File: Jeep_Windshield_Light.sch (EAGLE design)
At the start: 9 parts

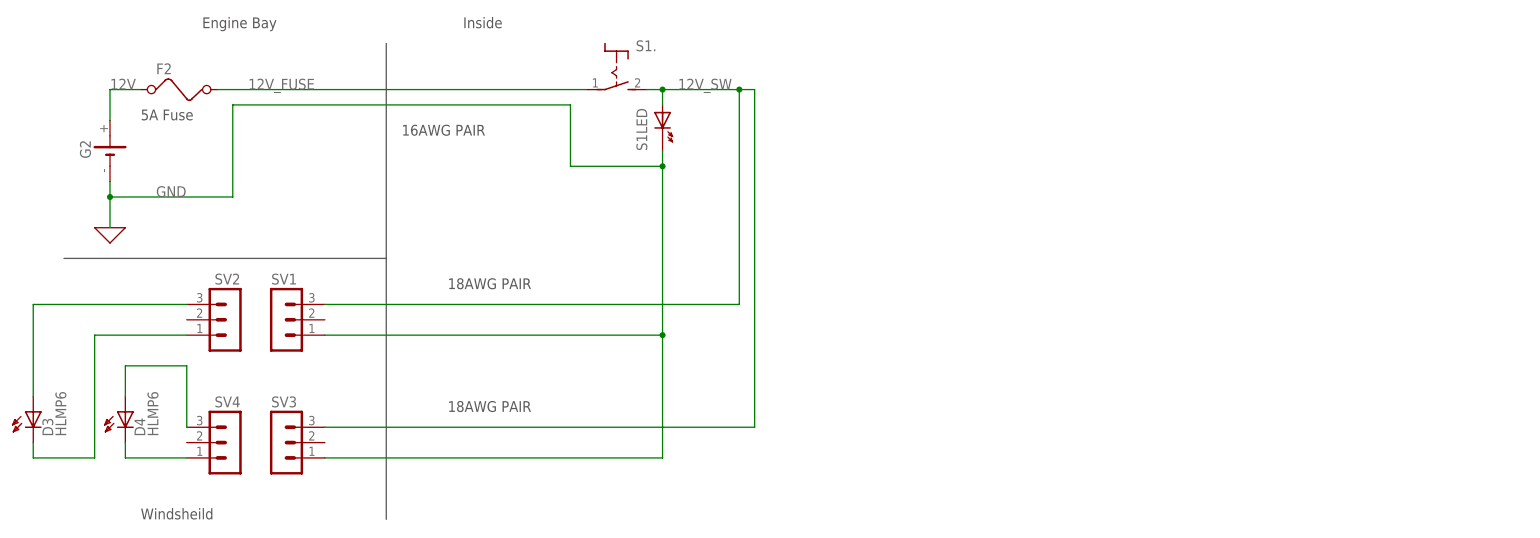
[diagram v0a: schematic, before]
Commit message: Updating grill version to include the ignition wiring. Also updating the original version to look consistent.
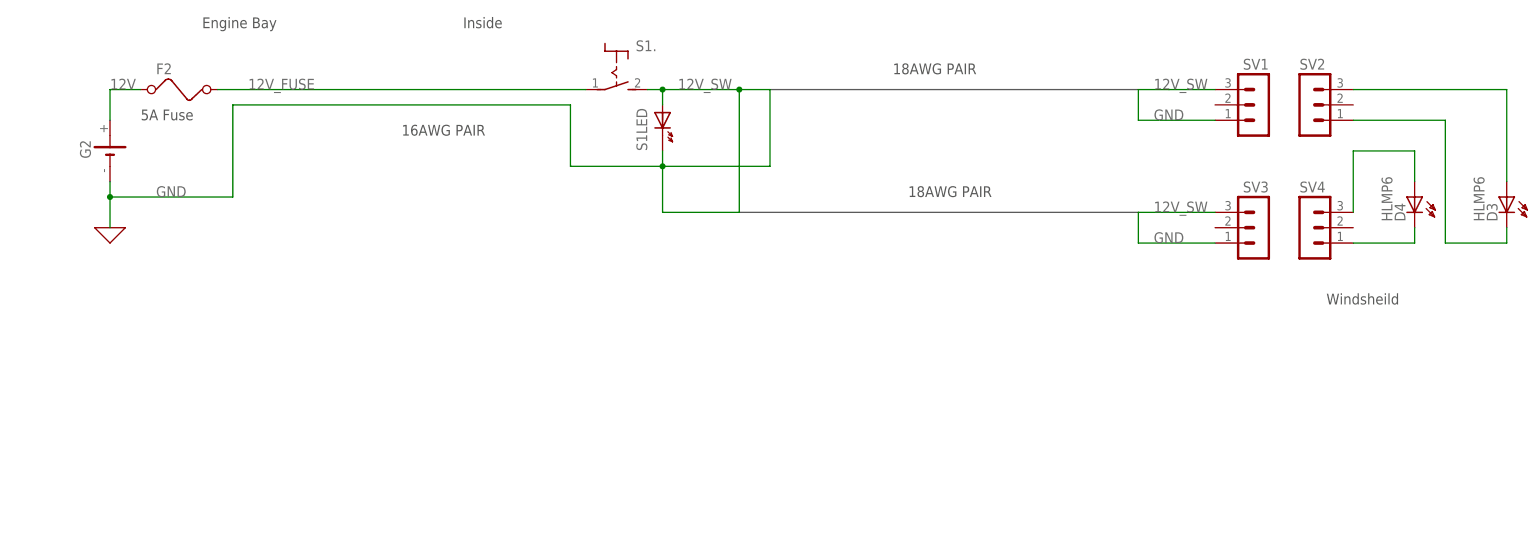
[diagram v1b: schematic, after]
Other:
- moved on the sheet: D3, D4, SV1, SV2, SV3, SV4
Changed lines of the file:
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@@
 <plain>
 <text x="22.86" y="63.5" size="1.778" layer="97">5A Fuse</text>
-<wire x1="63.5" y1="76.2" x2="63.5" y2="40.64" width="0.1524" layer="97"/>
 <text x="76.2" y="78.74" size="1.778" layer="97">Inside</text>
 <text x="33.02" y="78.74" size="1.778" layer="97">Engine Bay</text>
-<wire x1="63.5" y1="40.64" x2="63.5" y2="-2.54" width="0.1524" layer="97"/>
-<wire x1="10.16" y1="40.64" x2="63.5" y2="40.64" width="0.1524" layer="97"/>
-<text x="22.86" y="-2.54" size="1.778" layer="97">Windsheild</text>
+<text x="231.14" y="33.02" size="1.778" layer="97" rot="MR0">Windsheild</text>
 <text x="66.04" y="60.96" size="1.778" layer="97">16AWG PAIR</text>
-<text x="73.66" y="35.56" size="1.778" layer="97">18AWG PAIR</text>
-<text x="73.66" y="15.24" size="1.778" layer="97">18AWG PAIR</text>
+<text x="147.32" y="71.12" size="1.778" layer="97">18AWG PAIR</text>
+<text x="149.86" y="50.8" size="1.778" layer="97">18AWG PAIR</text>
 </plain>
 <instances>
@@
 <instance part="S1" gate="LED" x="109.22" y="63.5"/>
 <instance part="X_2" gate="G$1" x="17.78" y="45.72"/>
-<instance part="D3" gate="A" x="5.08" y="12.7"/>
-<instance part="D4" gate="A" x="20.32" y="12.7"/>
-<instance part="SV1" gate="G$1" x="45.72" y="30.48"/>
-<instance part="SV2" gate="G$1" x="38.1" y="30.48" rot="MR0"/>
-<instance part="SV3" gate="G$1" x="45.72" y="10.16"/>
-<instance part="SV4" gate="G$1" x="38.1" y="10.16" rot="MR0"/>
+<instance part="D3" gate="A" x="248.92" y="48.26" rot="MR0"/>
+<instance part="D4" gate="A" x="233.68" y="48.26" rot="MR0"/>
+<instance part="SV1" gate="G$1" x="208.28" y="66.04" rot="MR0"/>
+<instance part="SV2" gate="G$1" x="215.9" y="66.04"/>
+<instance part="SV3" gate="G$1" x="208.28" y="45.72" rot="MR0"/>
+<instance part="SV4" gate="G$1" x="215.9" y="45.72"/>
 </instances>
 <busses>
+<bus name="12V_SW,GND">
+<segment>
+<wire x1="127" y1="68.58" x2="187.96" y2="68.58" width="0.762" layer="92"/>
+</segment>
+<segment>
+<wire x1="121.92" y1="48.26" x2="187.96" y2="48.26" width="0.762" layer="92"/>
+</segment>
+</bus>
 </busses>
 <nets>
@@
 </segment>
 </net>
-<net name="12V_SW" class="0">
-<segment>
-<pinref part="S1" gate="." pin="S"/>
-<wire x1="106.68" y1="68.58" x2="109.22" y2="68.58" width="0.1524" layer="91"/>
-<wire x1="109.22" y1="68.58" x2="121.92" y2="68.58" width="0.1524" layer="91"/>
-<wire x1="109.22" y1="66.04" x2="109.22" y2="68.58" width="0.1524" layer="91"/>
-<junction x="109.22" y="68.58"/>
-<pinref part="S1" gate="LED" pin="A"/>
-<wire x1="121.92" y1="68.58" x2="121.92" y2="33.02" width="0.1524" layer="91"/>
-<wire x1="124.46" y1="68.58" x2="124.46" y2="12.7" width="0.1524" layer="91"/>
-<wire x1="124.46" y1="68.58" x2="121.92" y2="68.58" width="0.1524" layer="91"/>
-<junction x="121.92" y="68.58"/>
-<pinref part="SV1" gate="G$1" pin="3"/>
-<wire x1="53.34" y1="33.02" x2="121.92" y2="33.02" width="0.1524" layer="91"/>
-<pinref part="SV3" gate="G$1" pin="3"/>
-<wire x1="53.34" y1="12.7" x2="124.46" y2="12.7" width="0.1524" layer="91"/>
-<label x="111.76" y="68.58" size="1.778" layer="95"/>
-</segment>
-</net>
 <net name="GND" class="0">
 <segment>
@@
 <wire x1="17.78" y1="45.72" x2="17.78" y2="50.8" width="0.1524" layer="91"/>
 <junction x="17.78" y="50.8"/>
-<wire x1="109.22" y1="55.88" x2="109.22" y2="27.94" width="0.1524" layer="91"/>
 <junction x="109.22" y="55.88"/>
+<wire x1="109.22" y1="55.88" x2="109.22" y2="48.26" width="0.1524" layer="91"/>
+<wire x1="109.22" y1="55.88" x2="127" y2="55.88" width="0.1524" layer="91"/>
+<wire x1="127" y1="55.88" x2="127" y2="68.58" width="0.1524" layer="91"/>
+<wire x1="121.92" y1="48.26" x2="109.22" y2="48.26" width="0.1524" layer="91"/>
+</segment>
+<segment>
 <pinref part="SV1" gate="G$1" pin="1"/>
-<wire x1="53.34" y1="27.94" x2="109.22" y2="27.94" width="0.1524" layer="91"/>
+<wire x1="187.96" y1="63.5" x2="200.66" y2="63.5" width="0.1524" layer="91"/>
+<label x="190.5" y="63.5" size="1.778" layer="95"/>
+<wire x1="187.96" y1="63.5" x2="187.96" y2="68.58" width="0.1524" layer="91"/>
+</segment>
+<segment>
+<wire x1="187.96" y1="48.26" x2="187.96" y2="43.18" width="0.1524" layer="91"/>
 <pinref part="SV3" gate="G$1" pin="1"/>
-<wire x1="53.34" y1="7.62" x2="109.22" y2="7.62" width="0.1524" layer="91"/>
-<wire x1="109.22" y1="27.94" x2="109.22" y2="7.62" width="0.1524" layer="91"/>
-<junction x="109.22" y="27.94"/>
+<wire x1="187.96" y1="43.18" x2="200.66" y2="43.18" width="0.1524" layer="91"/>
+<label x="190.5" y="43.18" size="1.778" layer="95"/>
 </segment>
 </net>
@@
 <segment>
 <pinref part="D4" gate="A" pin="A"/>
-<wire x1="20.32" y1="22.86" x2="20.32" y2="17.78" width="0.1524" layer="91"/>
+<wire x1="233.68" y1="58.42" x2="233.68" y2="53.34" width="0.1524" layer="91"/>
 <pinref part="SV4" gate="G$1" pin="3"/>
-<wire x1="30.48" y1="12.7" x2="30.48" y2="22.86" width="0.1524" layer="91"/>
-<wire x1="30.48" y1="22.86" x2="20.32" y2="22.86" width="0.1524" layer="91"/>
+<wire x1="223.52" y1="48.26" x2="223.52" y2="58.42" width="0.1524" layer="91"/>
+<wire x1="223.52" y1="58.42" x2="233.68" y2="58.42" width="0.1524" layer="91"/>
 </segment>
 </net>
@@
 <pinref part="D3" gate="A" pin="A"/>
 <pinref part="SV2" gate="G$1" pin="3"/>
-<wire x1="30.48" y1="33.02" x2="5.08" y2="33.02" width="0.1524" layer="91"/>
-<wire x1="5.08" y1="33.02" x2="5.08" y2="17.78" width="0.1524" layer="91"/>
+<wire x1="223.52" y1="68.58" x2="248.92" y2="68.58" width="0.1524" layer="91"/>
+<wire x1="248.92" y1="68.58" x2="248.92" y2="53.34" width="0.1524" layer="91"/>
 </segment>
 </net>
@@
 <pinref part="D4" gate="A" pin="K"/>
 <pinref part="SV4" gate="G$1" pin="1"/>
-<wire x1="20.32" y1="7.62" x2="20.32" y2="10.16" width="0.1524" layer="91"/>
-<wire x1="30.48" y1="7.62" x2="20.32" y2="7.62" width="0.1524" layer="91"/>
+<wire x1="233.68" y1="43.18" x2="233.68" y2="45.72" width="0.1524" layer="91"/>
+<wire x1="223.52" y1="43.18" x2="233.68" y2="43.18" width="0.1524" layer="91"/>
 </segment>
 </net>
@@
 <segment>
 <pinref part="D3" gate="A" pin="K"/>
-<wire x1="5.08" y1="7.62" x2="5.08" y2="10.16" width="0.1524" layer="91"/>
+<wire x1="248.92" y1="43.18" x2="248.92" y2="45.72" width="0.1524" layer="91"/>
 <pinref part="SV2" gate="G$1" pin="1"/>
-<wire x1="30.48" y1="27.94" x2="15.24" y2="27.94" width="0.1524" layer="91"/>
-<wire x1="15.24" y1="27.94" x2="15.24" y2="7.62" width="0.1524" layer="91"/>
-<wire x1="15.24" y1="7.62" x2="5.08" y2="7.62" width="0.1524" layer="91"/>
+<wire x1="223.52" y1="63.5" x2="238.76" y2="63.5" width="0.1524" layer="91"/>
+<wire x1="238.76" y1="63.5" x2="238.76" y2="43.18" width="0.1524" layer="91"/>
+<wire x1="238.76" y1="43.18" x2="248.92" y2="43.18" width="0.1524" layer="91"/>
 </segment>
 </net>
+<net name="B$1" class="0">
+<segment>
+<wire x1="193.04" y1="68.58" x2="187.96" y2="68.58" width="0.1524" layer="91"/>
+</segment>
+</net>
+<net name="12V_SW" class="0">
+<segment>
+<pinref part="SV1" gate="G$1" pin="3"/>
+<wire x1="193.04" y1="68.58" x2="200.66" y2="68.58" width="0.1524" layer="91"/>
+<label x="190.5" y="68.58" size="1.778" layer="95"/>
+</segment>
+<segment>
+<pinref part="SV3" gate="G$1" pin="3"/>
+<wire x1="187.96" y1="48.26" x2="200.66" y2="48.26" width="0.1524" layer="91"/>
+<label x="190.5" y="48.26" size="1.778" layer="95"/>
+</segment>
+<segment>
+<pinref part="S1" gate="." pin="S"/>
+<wire x1="106.68" y1="68.58" x2="109.22" y2="68.58" width="0.1524" layer="91"/>
+<wire x1="109.22" y1="66.04" x2="109.22" y2="68.58" width="0.1524" layer="91"/>
+<pinref part="S1" gate="LED" pin="A"/>
+<label x="111.76" y="68.58" size="1.778" layer="95"/>
+<wire x1="127" y1="68.58" x2="121.92" y2="68.58" width="0.1524" layer="91"/>
+<junction x="109.22" y="68.58"/>
+<wire x1="121.92" y1="68.58" x2="109.22" y2="68.58" width="0.1524" layer="91"/>
+<wire x1="121.92" y1="48.26" x2="121.92" y2="68.58" width="0.1524" layer="91"/>
+<junction x="121.92" y="68.58"/>
+</segment>
+</net>
